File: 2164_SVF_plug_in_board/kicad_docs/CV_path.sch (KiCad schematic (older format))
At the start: 11 parts, among them U4 TL072

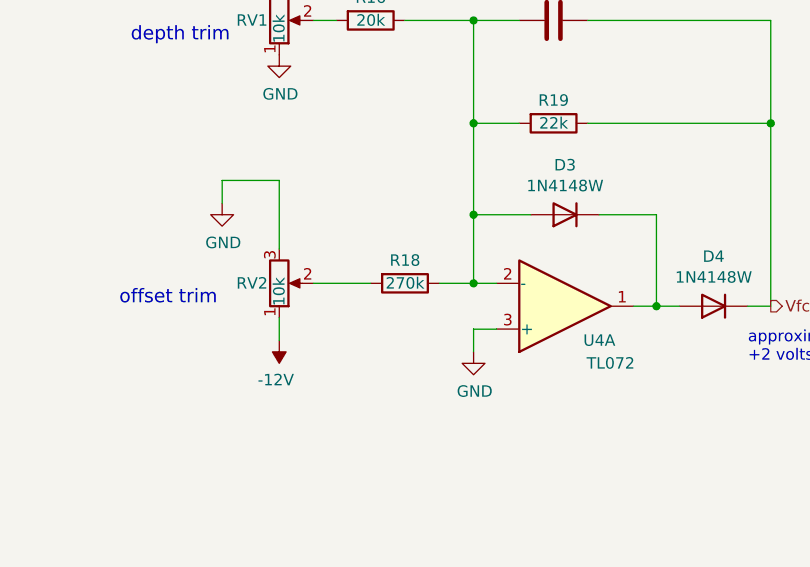
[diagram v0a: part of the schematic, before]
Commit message: change Fcv offset trim resistor
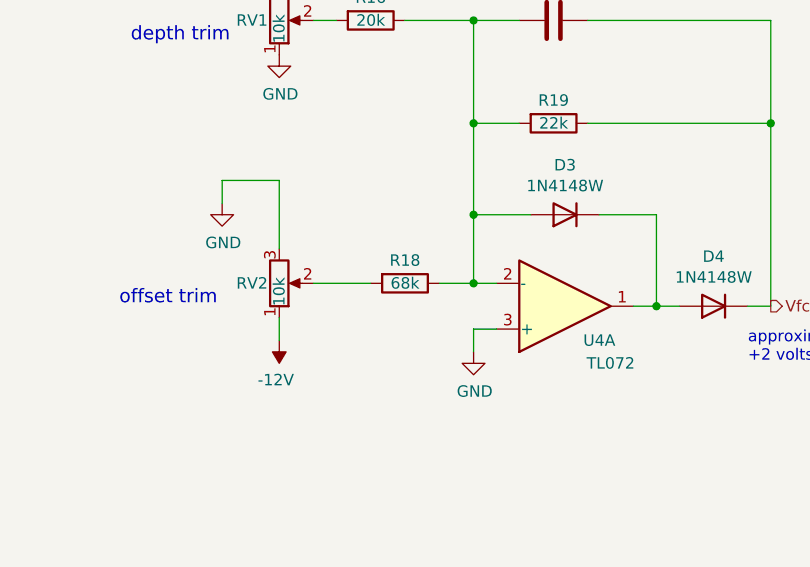
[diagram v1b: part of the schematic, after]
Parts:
- R18: value 270k -> 68k
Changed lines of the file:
@@
 P 2600 4150
 F 0 "R18" V 2500 4150 50  0000 C CNN
-F 1 "270k" V 2600 4150 50  0000 C CNN
+F 1 "68k" V 2600 4150 50  0000 C CNN
 F 2 "Resistor_SMD:R_0805_2012Metric_Pad1.15x1.40mm_HandSolder" V 2530 4150 50  0001 C CNN
 F 3 "~" H 2600 4150 50  0001 C CNN
